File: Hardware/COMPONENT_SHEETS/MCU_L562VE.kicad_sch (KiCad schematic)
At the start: 20 parts, among them U6 STM32L562VET, Y1 32MHz

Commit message: Corrected clock crystal on MCU
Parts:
- Y1: footprint Crystal:Crystal_SMD_2012-2Pin_2.0x1.2mm_HandSoldering -> RDT_Custom_Footprints:XTAL_ABM7-32.000MHZ-D2Y-T
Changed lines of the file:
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@@
     (effects (font (size 1.27 1.27)) (justify left))
   )
-  (symbol (lib_id "power:+3.3V") (at 167.64 33.02 0)
+  (symbol (lib_id "power:+3.3V") (at 167.64 33.02 0) (unit 1)
     (in_bom yes) (on_board yes)
     (property "Reference" "#PWR035" (id 0) (at 167.64 36.83 0)
@@
     (pin "1")
   )
-  (symbol (lib_id "Device:C_Small") (at 167.64 38.1 0)
+  (symbol (lib_id "Device:C_Small") (at 167.64 38.1 0) (unit 1)
     (in_bom yes) (on_board yes)
     (property "Reference" "C26" (id 0) (at 169.9768 36.9316 0)
@@
     (pin "2")
   )
-  (symbol (lib_id "Device:C_Small") (at 177.8 38.1 0)
+  (symbol (lib_id "Device:C_Small") (at 177.8 38.1 0) (unit 1)
     (in_bom yes) (on_board yes)
     (property "Reference" "C27" (id 0) (at 180.1368 36.9316 0)
@@
     (pin "2")
   )
-  (symbol (lib_id "Device:C_Small") (at 189.23 38.1 0)
+  (symbol (lib_id "Device:C_Small") (at 189.23 38.1 0) (unit 1)
     (in_bom yes) (on_board yes)
     (property "Reference" "C28" (id 0) (at 191.5668 36.9316 0)
@@
     (pin "2")
   )
-  (symbol (lib_id "Device:C_Small") (at 223.52 38.1 0)
+  (symbol (lib_id "Device:C_Small") (at 223.52 38.1 0) (unit 1)
     (in_bom yes) (on_board yes)
     (property "Reference" "C31" (id 0) (at 225.8568 36.9316 0)
@@
     (pin "2")
   )
-  (symbol (lib_id "Device:C_Small") (at 269.24 38.1 0)
+  (symbol (lib_id "Device:C_Small") (at 269.24 38.1 0) (unit 1)
     (in_bom yes) (on_board yes)
     (property "Reference" "C35" (id 0) (at 271.5768 36.9316 0)
@@
     (pin "2")
   )
-  (symbol (lib_id "power:GND") (at 167.64 43.18 0)
+  (symbol (lib_id "power:GND") (at 167.64 43.18 0) (unit 1)
     (in_bom yes) (on_board yes)
     (property "Reference" "#PWR036" (id 0) (at 167.64 49.53 0)
@@
     (pin "1")
   )
-  (symbol (lib_id "power:+3.3V") (at 187.96 82.55 0)
+  (symbol (lib_id "power:+3.3V") (at 187.96 82.55 0) (unit 1)
     (in_bom yes) (on_board yes)
     (property "Reference" "#PWR037" (id 0) (at 187.96 86.36 0)
@@
     (pin "1")
   )
-  (symbol (lib_id "Device:R_Small") (at 193.04 88.9 270)
+  (symbol (lib_id "Device:R_Small") (at 193.04 88.9 270) (unit 1)
     (in_bom yes) (on_board yes)
     (property "Reference" "R18" (id 0) (at 193.04 83.9216 90))
@@
     (pin "2")
   )
-  (symbol (lib_id "Device:R_Small") (at 193.04 96.52 270)
+  (symbol (lib_id "Device:R_Small") (at 193.04 96.52 270) (unit 1)
     (in_bom yes) (on_board yes)
     (property "Reference" "R19" (id 0) (at 193.04 91.5416 90))
@@
     (pin "1")
   )
-  (symbol (lib_id "Device:C_Small") (at 200.66 38.1 0)
+  (symbol (lib_id "Device:C_Small") (at 200.66 38.1 0) (unit 1)
     (in_bom yes) (on_board yes)
     (property "Reference" "C29" (id 0) (at 202.9968 36.9316 0)
@@
     (pin "2")
   )
-  (symbol (lib_id "Device:C_Small") (at 212.09 38.1 0)
+  (symbol (lib_id "Device:C_Small") (at 212.09 38.1 0) (unit 1)
     (in_bom yes) (on_board yes)
     (property "Reference" "C30" (id 0) (at 214.4268 36.9316 0)
@@
     (pin "2")
   )
-  (symbol (lib_id "Device:C_Small") (at 234.95 38.1 0)
+  (symbol (lib_id "Device:C_Small") (at 234.95 38.1 0) (unit 1)
     (in_bom yes) (on_board yes)
     (property "Reference" "C32" (id 0) (at 237.2868 36.9316 0)
@@
     (pin "2")
   )
-  (symbol (lib_id "Device:C_Small") (at 246.38 38.1 0)
+  (symbol (lib_id "Device:C_Small") (at 246.38 38.1 0) (unit 1)
     (in_bom yes) (on_board yes)
     (property "Reference" "C33" (id 0) (at 248.7168 36.9316 0)
@@
     (pin "2")
   )
-  (symbol (lib_id "Device:C_Small") (at 257.81 38.1 0)
+  (symbol (lib_id "Device:C_Small") (at 257.81 38.1 0) (unit 1)
     (in_bom yes) (on_board yes)
     (property "Reference" "C34" (id 0) (at 260.1468 36.9316 0)
@@
     (pin "2")
   )
-  (symbol (lib_id "Device:C_Small") (at 29.21 87.63 0)
+  (symbol (lib_id "Device:C_Small") (at 29.21 87.63 0) (unit 1)
     (in_bom yes) (on_board yes)
     (property "Reference" "C24" (id 0) (at 31.5468 86.4616 0)
@@
     (pin "2")
   )
-  (symbol (lib_id "Device:C_Small") (at 39.37 87.63 0)
+  (symbol (lib_id "Device:C_Small") (at 39.37 87.63 0) (unit 1)
     (in_bom yes) (on_board yes)
     (property "Reference" "C25" (id 0) (at 41.7068 86.4616 0)
@@
     (pin "2")
   )
-  (symbol (lib_id "Device:Crystal_Small") (at 34.29 82.55 0)
+  (symbol (lib_id "Device:Crystal_Small") (at 34.29 82.55 0) (unit 1)
     (in_bom yes) (on_board yes)
     (property "Reference" "Y1" (id 0) (at 34.29 76.835 0))
     (property "Value" "32MHz" (id 1) (at 34.29 79.1464 0))
-    (property "Footprint" "Crystal:Crystal_SMD_2012-2Pin_2.0x1.2mm_HandSoldering" (id 2) (at 34.29 82.55 0)
+    (property "Footprint" "RDT_Custom_Footprints:XTAL_ABM7-32.000MHZ-D2Y-T" (id 2) (at 34.29 82.55 0)
       (effects (font (size 1.27 1.27)) hide)
     )
@@
     (pin "2")
   )
-  (symbol (lib_id "Device:R") (at 134.62 82.55 0) (mirror y)
+  (symbol (lib_id "Device:R") (at 134.62 82.55 0) (mirror y) (unit 1)
     (in_bom yes) (on_board yes)
     (property "Reference" "R17" (id 0) (at 132.842 81.3816 0)
@@
     (pin "2")
   )
-  (symbol (lib_id "Device:LED") (at 134.62 72.39 270) (mirror x)
+  (symbol (lib_id "Device:LED") (at 134.62 72.39 270) (mirror x) (unit 1)
     (in_bom yes) (on_board yes)
     (property "Reference" "D6" (id 0) (at 131.6228 71.3994 90)
@@
     (pin "2")
   )
-  (symbol (lib_id "Device:LED") (at 125.73 72.39 270) (mirror x)
+  (symbol (lib_id "Device:LED") (at 125.73 72.39 270) (mirror x) (unit 1)
     (in_bom yes) (on_board yes)
     (property "Reference" "D5" (id 0) (at 122.7328 71.3994 90)
@@
     (pin "2")
   )
-  (symbol (lib_id "Device:R") (at 125.73 82.55 0) (mirror y)
+  (symbol (lib_id "Device:R") (at 125.73 82.55 0) (mirror y) (unit 1)
     (in_bom yes) (on_board yes)
     (property "Reference" "R16" (id 0) (at 123.952 81.3816 0)

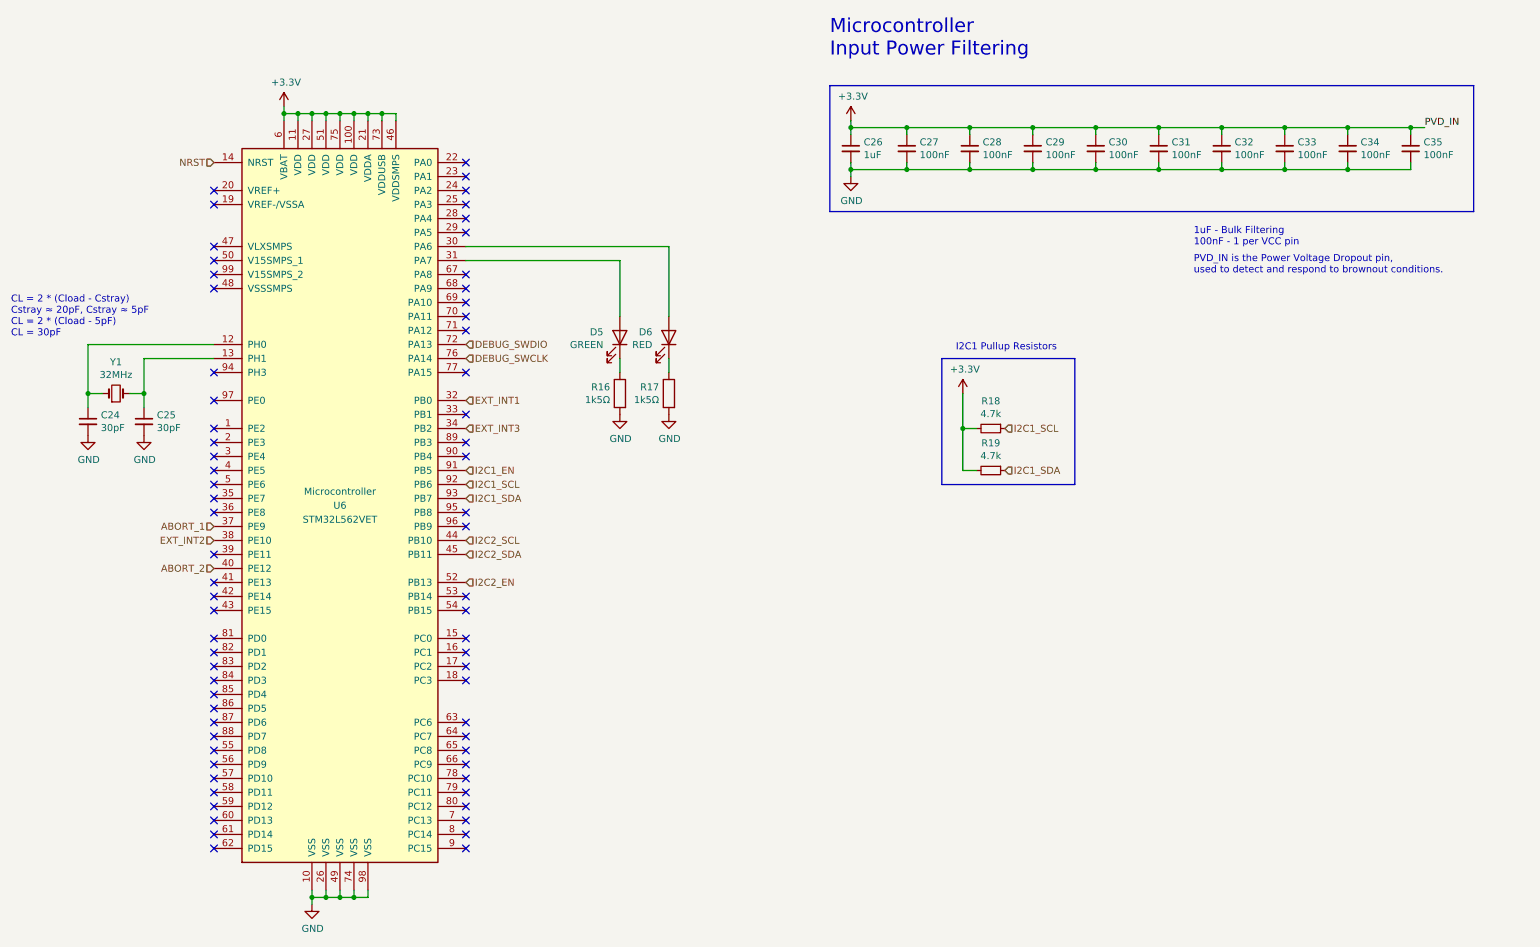
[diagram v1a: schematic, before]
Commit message: Separated I2C Lines
For better EMI/EMC mitigation.
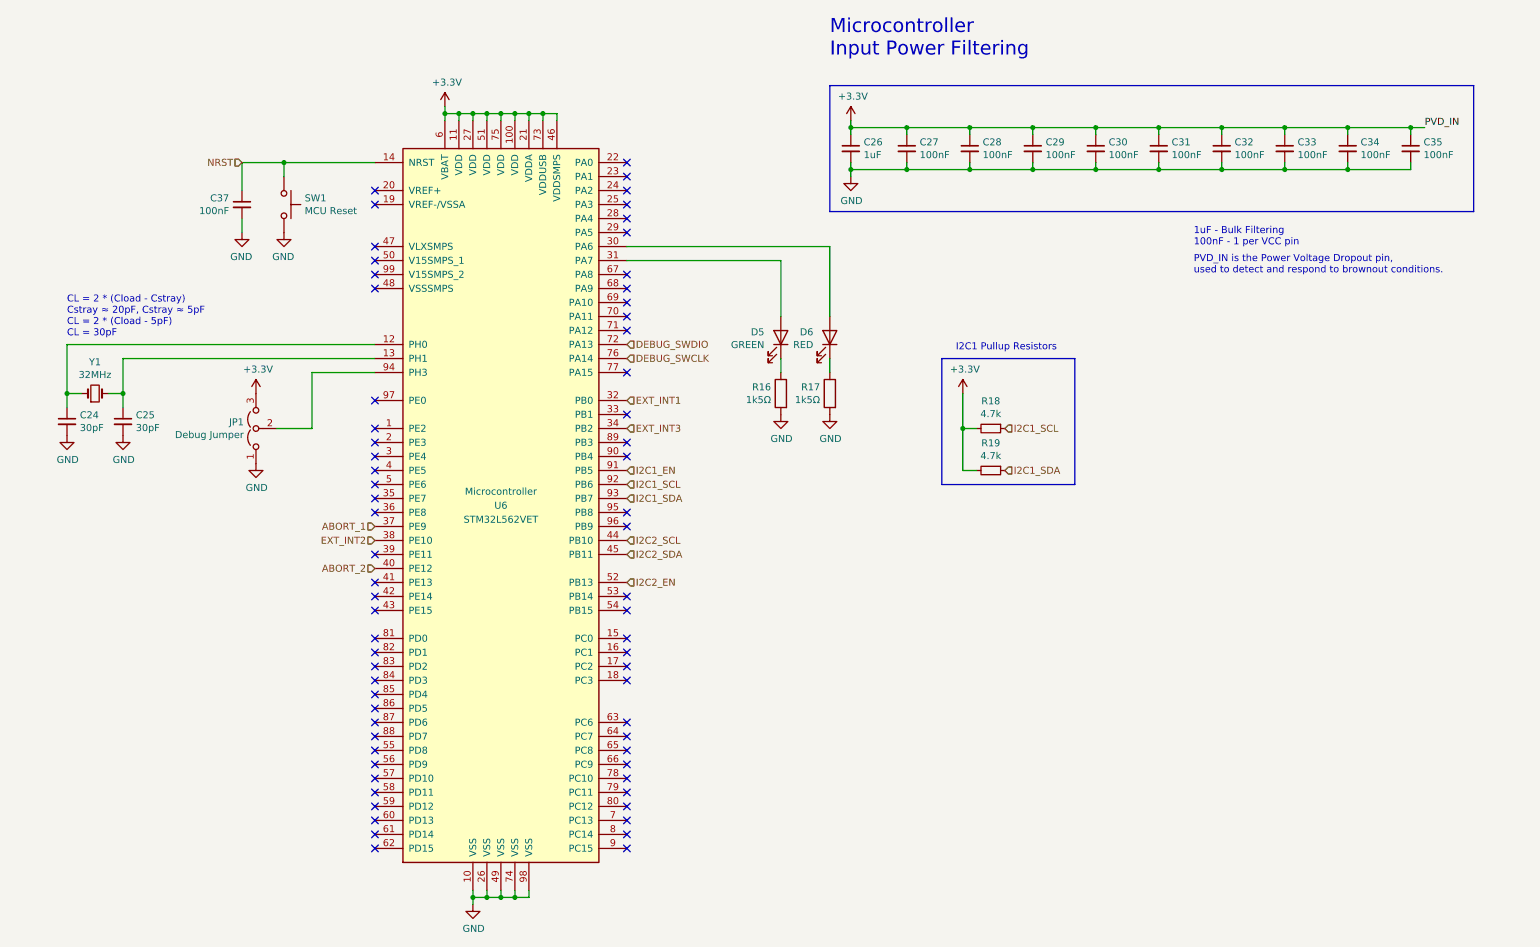
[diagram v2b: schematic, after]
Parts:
- added C37: 100nF, Capacitor_SMD:C_0603_1608Metric_Pad1.08x0.95mm_HandSolder, symbol Device:C_Small
- added JP1: Debug Jumper, Connector_PinHeader_2.54mm:PinHeader_1x03_P2.54mm_Vertical, symbol Jumper:Jumper_3_Open
- added SW1: MCU Reset, Button_Switch_SMD:SW_SPST_PTS645, symbol Switch:SW_Push
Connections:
- net +3V3: now also JP1.3 (B)
- net GND: now also C37.2, JP1.1 (A), SW1.2
- net NRST: now also C37.1, SW1.1
- net at U6.94 (PH3): now also JP1.2 (C)
- no-connect marks 68 -> 67
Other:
- moved on the sheet: C24, C25, D5, D6, R16, R17, U6, Y1

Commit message: Added bootloader pins, adjusted lipo monitor and mcu buttons
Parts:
- renumbered C37 to C36
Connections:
- net EXT_INT2: now also U6.77 (PA15); no longer U6.38 (PE10)
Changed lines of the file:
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@@
   (no_connect (at 81.28 99.06))
   (no_connect (at 127 71.12))
+  (no_connect (at 81.28 109.22))
   (no_connect (at 127 157.48))
-  (no_connect (at 127 78.74))
   (no_connect (at 81.28 149.86))
   (no_connect (at 127 142.24))
@@
     (effects (font (size 1.27 1.27)) (justify left))
   )
-  (hierarchical_label "EXT_INT2" (shape input) (at 81.28 109.22 180)
-    (effects (font (size 1.27 1.27)) (justify right))
+  (hierarchical_label "EXT_INT2" (shape input) (at 127 78.74 0)
+    (effects (font (size 1.27 1.27)) (justify left))
   )
   (hierarchical_label "I2C1_SCL" (shape input) (at 195.58 88.9 0)
@@
   (symbol (lib_id "Device:C_Small") (at 57.15 48.26 0) (mirror y) (unit 1)
     (in_bom yes) (on_board yes)
-    (property "Reference" "C37" (id 0) (at 54.8132 47.0916 0)
-      (effects (font (size 1.27 1.27)) (justify left))
-    )
+    (property "Reference" "C36" (id 0) (at 54.8132 47.0916 0)
+      (effects (font (size 1.27 1.27)) (justify left))
+    )
